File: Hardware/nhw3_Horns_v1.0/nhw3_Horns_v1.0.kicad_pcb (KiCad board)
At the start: 2 copper layers, 0 parts

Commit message: Finished Horns Board Layout
Fixed half-first order RC filter on MOSFET, finished PCB layout. Ran DRC with no errors.
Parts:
- added C10: 100μF, Capacitor_SMD:C_0603_1608Metric_Pad1.08x0.95mm_HandSolder, F.Cu at (178.9, 141.3)
- added C2: 0.1μF, Capacitor_SMD:C_0603_1608Metric_Pad1.08x0.95mm_HandSolder, F.Cu at (168.8, 119.9)
- added C3: 0.1μF, Capacitor_SMD:C_0603_1608Metric_Pad1.08x0.95mm_HandSolder, F.Cu at (165.2, 116.6)
- added C4: 0.1μF, Capacitor_SMD:C_0603_1608Metric_Pad1.08x0.95mm_HandSolder, F.Cu at (168.9, 116.6)
- added C5: 0.1μF, Capacitor_SMD:C_0603_1608Metric_Pad1.08x0.95mm_HandSolder, F.Cu at (174.9, 138.4)
- added C6: 1μF, Capacitor_SMD:C_0603_1608Metric_Pad1.08x0.95mm_HandSolder, F.Cu at (174.8, 141.3)
- added C7: 1μF, Capacitor_SMD:C_0603_1608Metric_Pad1.08x0.95mm_HandSolder, F.Cu at (158.2, 123.2)
- added C8: 10μF, Capacitor_SMD:C_0603_1608Metric_Pad1.08x0.95mm_HandSolder, F.Cu at (158.2, 126.2)
- added C9: 10μF, Capacitor_SMD:C_0603_1608Metric_Pad1.08x0.95mm_HandSolder, F.Cu at (178.9, 138.4)
- added D1: D, Diode_SMD:D_0603_1608Metric_Pad1.05x0.95mm_HandSolder, F.Cu at (173.4, 133.5)
- added F1: 2A, Fuse:Fuse_0603_1608Metric_Pad1.05x0.95mm_HandSolder, F.Cu at (174.3, 129.2)
- added F2: 2A, Fuse:Fuse_0603_1608Metric_Pad1.05x0.95mm_HandSolder, F.Cu at (161.0, 124.3)
- added J1: Conn_01x03, Connector_Molex:Molex_KK-254_AE-6410-03A_1x03_P2.54mm_Vertical, F.Cu at (165.1, 139.9)
- added J2: Conn_01x02, Connector_Molex:Molex_KK-254_AE-6410-02A_1x02_P2.54mm_Vertical, F.Cu at (159.7, 131.0)
- added J3: Conn_01x02, Connector_Molex:Molex_KK-254_AE-6410-02A_1x02_P2.54mm_Vertical, F.Cu at (166.8, 131.0)
- added J4: Conn_01x02, Connector_Molex:Molex_KK-254_AE-6410-02A_1x02_P2.54mm_Vertical, F.Cu at (177.7, 131.0)
- added Q1: Q_NMOS_GDS, layout:TO-252-2, F.Cu at (176.7, 122.2)
- added R2: 1kΩ, Resistor_SMD:R_0603_1608Metric_Pad0.98x0.95mm_HandSolder, F.Cu at (164.6, 119.9)
- added REF**: MountingHole_3.2mm_M3, MountingHole:MountingHole_3.2mm_M3, F.Cu at (158.8, 140.3)
- added REF**: MountingHole_3.2mm_M3, MountingHole:MountingHole_3.2mm_M3, F.Cu at (158.8, 116.8)
- added REF**: MountingHole_3.2mm_M3, MountingHole:MountingHole_3.2mm_M3, F.Cu at (185.8, 140.3)
- added REF**: MountingHole_3.2mm_M3, MountingHole:MountingHole_3.2mm_M3, F.Cu at (185.8, 116.8)
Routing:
- net GND: track 0.00 -> 23.8 mm, vias 0 -> 11
- net /HORN_CTRL: track 0.00 -> 23.1 mm
- net Net-(J3-Pin_1): track 0.00 -> 16.3 mm
- net /HORN_IN: track 0.00 -> 8.24 mm
- net Net-(Q1-D): track 0.00 -> 8.02 mm
- added copper zone on F.Cu, net +24V
- added copper zone on B.Cu, net GND
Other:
- board outline added: 36 x 36 mm

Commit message: Added push button to debug horns board
Added a push button in horns board schematic, assigned footprint, and updated pcb layout. Passed DRC with 0 errors.
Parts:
- added SW1: SW_Push, Button_Switch_SMD:SW_Push_1P1T_NO_CK_KMR2, F.Cu at (186.3, 130.0)
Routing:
- net Net-(Q1-D): track 8.02 -> 21.4 mm
- net GND: track 23.8 -> 29.5 mm, vias 11 -> 12

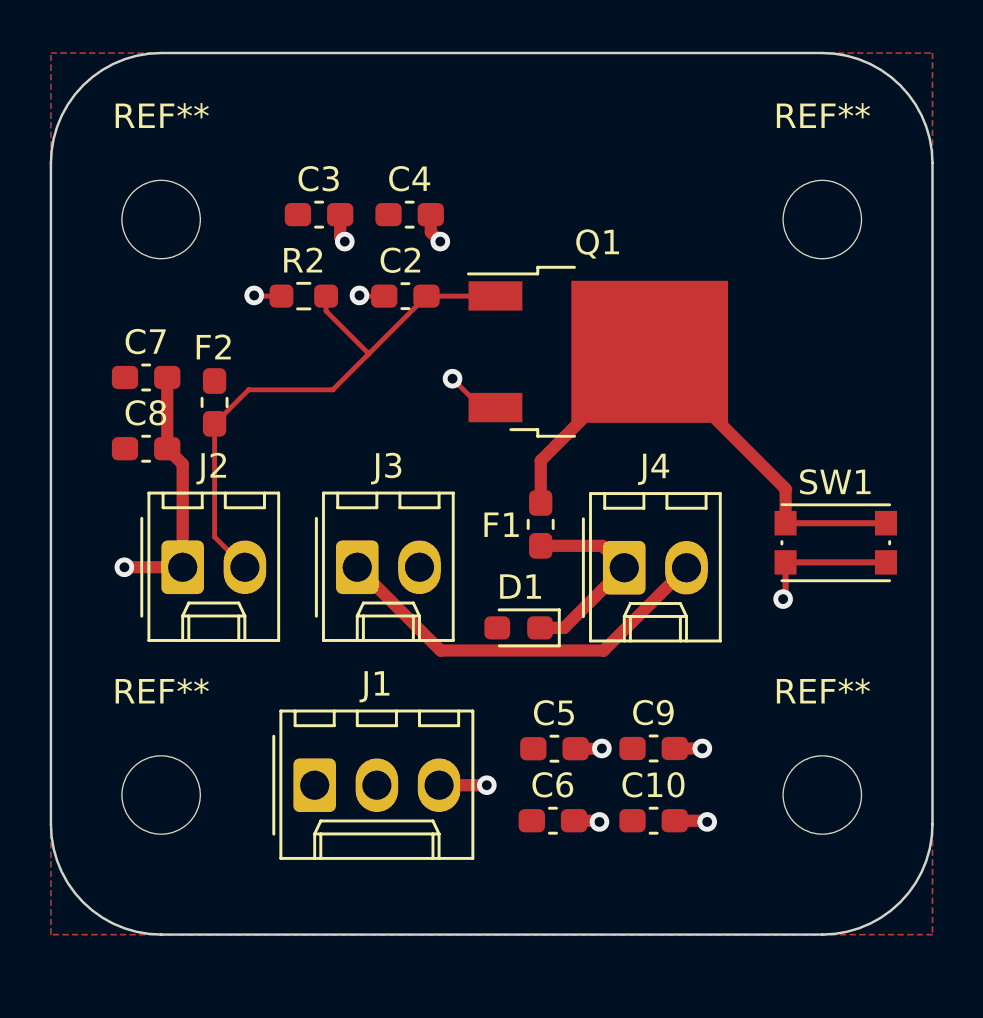
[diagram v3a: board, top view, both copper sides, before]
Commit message: Updated Connector Footprints
Changed from KK254 to Molex Micro-Fit Connector footprints. Updated layout as well, passed DRC with no errors or warnings.
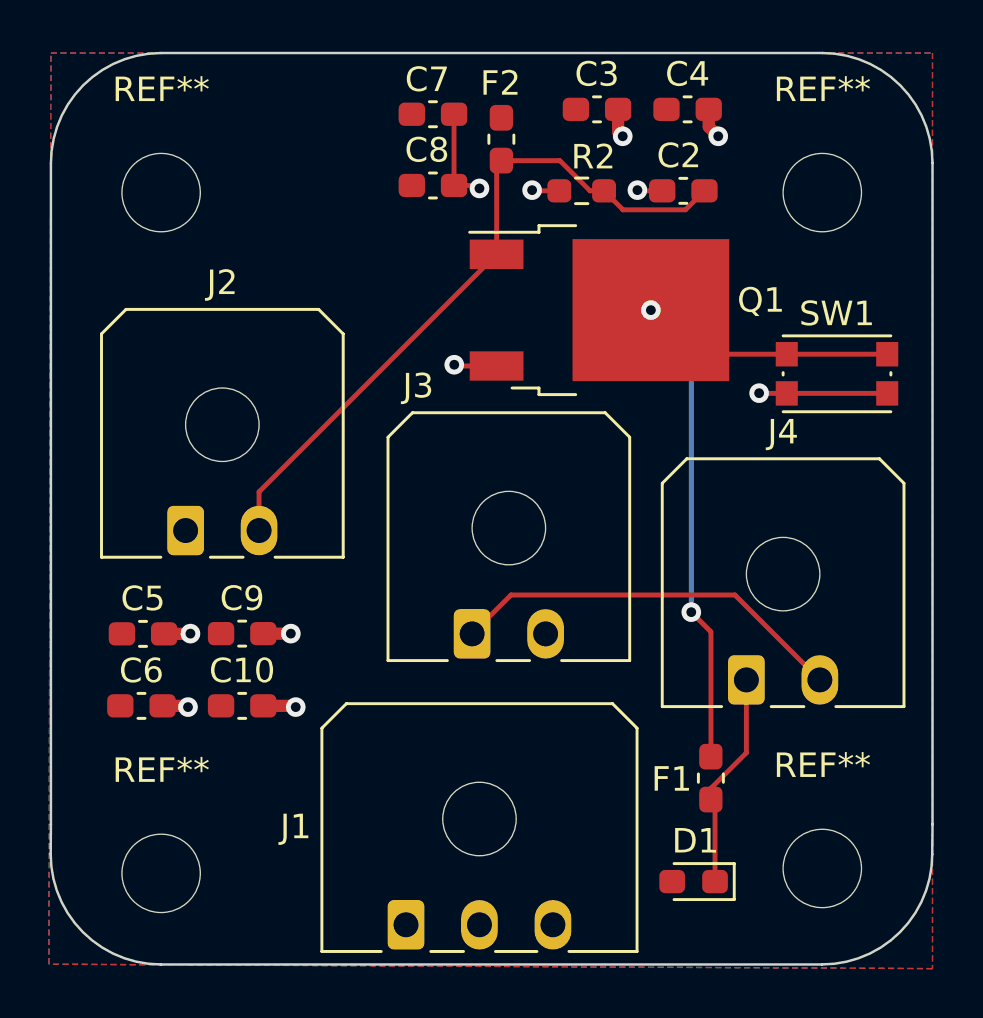
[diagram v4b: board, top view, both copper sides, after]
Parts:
- J1: footprint Connector_Molex:Molex_KK-254_AE-6410-03A_1x03_P2.54mm_Vertical -> Connector_Molex:Molex_Micro-Fit_3.0_43650-0300_1x03_P3.00mm_Horizontal
- J2, J3, J4: footprint Connector_Molex:Molex_KK-254_AE-6410-02A_1x02_P2.54mm_Vertical -> Connector_Molex:Molex_Micro-Fit_3.0_43650-0200_1x02_P3.00mm_Horizontal
- moved C5 17.4 mm to (158.1, 133.7)
- moved C6 17.4 mm to (158.0, 136.7)
- moved C10 17.4 mm to (162.1, 136.7)
- moved C9 17.4 mm to (162.1, 133.7)
- moved C7 15.9 mm to (169.9, 112.5)
- moved C8 15.9 mm to (169.9, 115.4)
- moved F2 15.9 mm to (172.7, 113.5)
- moved D1 12.6 mm to (180.5, 143.8)
- moved F1 12.5 mm to (181.2, 139.6)
- moved C4 12.1 mm to (180.3, 112.3)
- moved C2 12.1 mm to (180.1, 115.6)
- moved C3 12.1 mm to (176.6, 112.3)
- moved R2 12.1 mm to (176.0, 115.6)
- moved SW1 6.90 mm to (186.4, 123.1)
- moved J1 6.81 mm to (168.8, 145.6)
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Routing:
- net GND: track 29.5 -> 20.2 mm, vias 12 -> 11
- net Net-(Q1-D): track 21.4 -> 29.6 mm, vias 0 -> 2
- net /HORN_CTRL: track 23.1 -> 28.6 mm
- net /HORN_IN: track 8.24 -> 8.91 mm
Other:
- board size 36 x 36 mm -> 36 x 37.2 mm

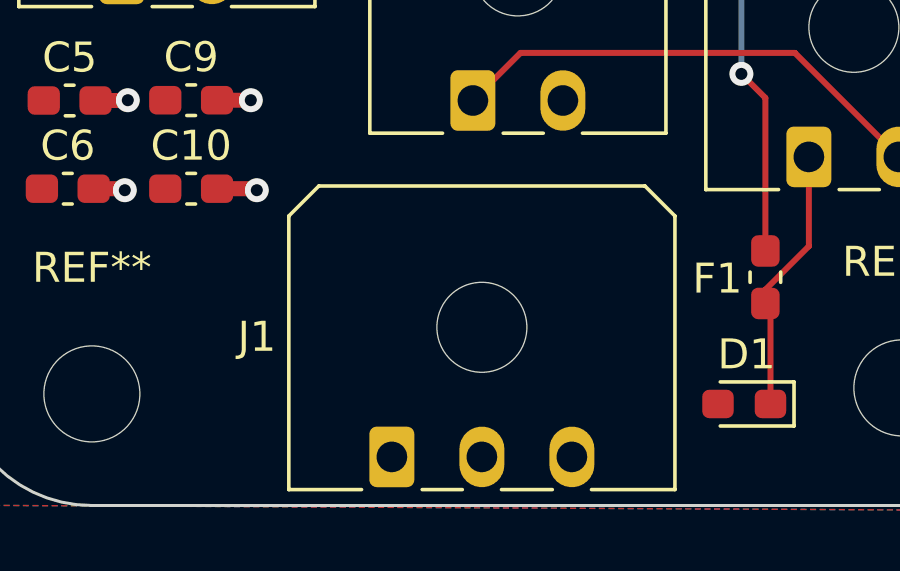
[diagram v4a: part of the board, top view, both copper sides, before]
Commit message: Updated User Drawings
Forgot to change User Drawing dimensions when modifying layout to fit new footprints.
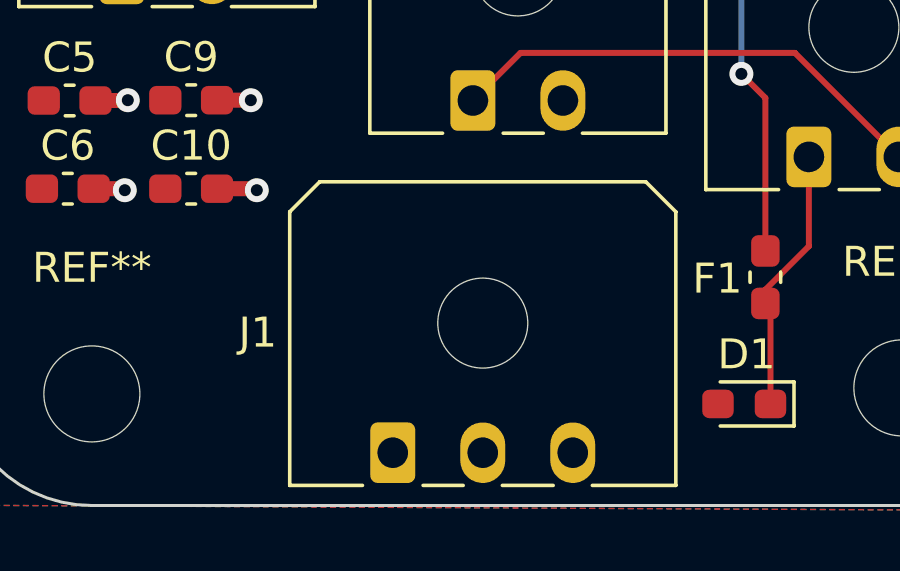
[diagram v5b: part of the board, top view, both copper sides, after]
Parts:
- moved J1 0.14 mm to (168.8, 145.5)
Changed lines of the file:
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@@
 	(footprint "Connector_Molex:Molex_Micro-Fit_3.0_43650-0300_1x03_P3.00mm_Horizontal"
 		(layer "F.Cu")
-		(at 168.8 145.6)
+		(at 168.83 145.46)
 		(descr "Molex Micro-Fit 3.0 Connector System, 43650-0300 (compatible alternatives: 43650-0301, 43650-0302), 3 Pins per row (https://www.molex.com/pdm_docs/sd/436500300_sd.pdf), generated with kicad-footprint-generator")
 		(tags "connector Molex Micro-Fit_3.0 top entry")
@@
 		(layer "Dwgs.User")
 		(pts
-			(xy 185.8 116.8) (xy 185.8 140.3)
+			(xy 185.8 115.7) (xy 185.8 143.3)
 		)
 		(height -9.3)
-		(gr_text "23.5000 mm"
-			(at 193.95 128.55 90)
+		(gr_text "27.6000 mm"
+			(at 193.95 129.5 90)
 			(layer "Dwgs.User")
 			(effects
@@
 		(layer "Dwgs.User")
 		(pts
-			(xy 154.3 146) (xy 154.3 110)
+			(xy 154.22 147.21) (xy 154.3 110)
 		)
 		(height -5.975)
-		(gr_text "36.0000 mm"
-			(at 147.175 128 90)
+		(gr_text "37.2101 mm"
+			(at 147.135017 128.589682 89.87681657)
 			(layer "Dwgs.User")
 			(effects
